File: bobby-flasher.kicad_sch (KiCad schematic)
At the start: 31 parts, among them J1 Conn_01x03, J2 Conn_01x06, J3 Flash, Q1 SS8050_C2150, Q2 SS8050_C2150, U1 CH343G, U2 AMS1117-3.3

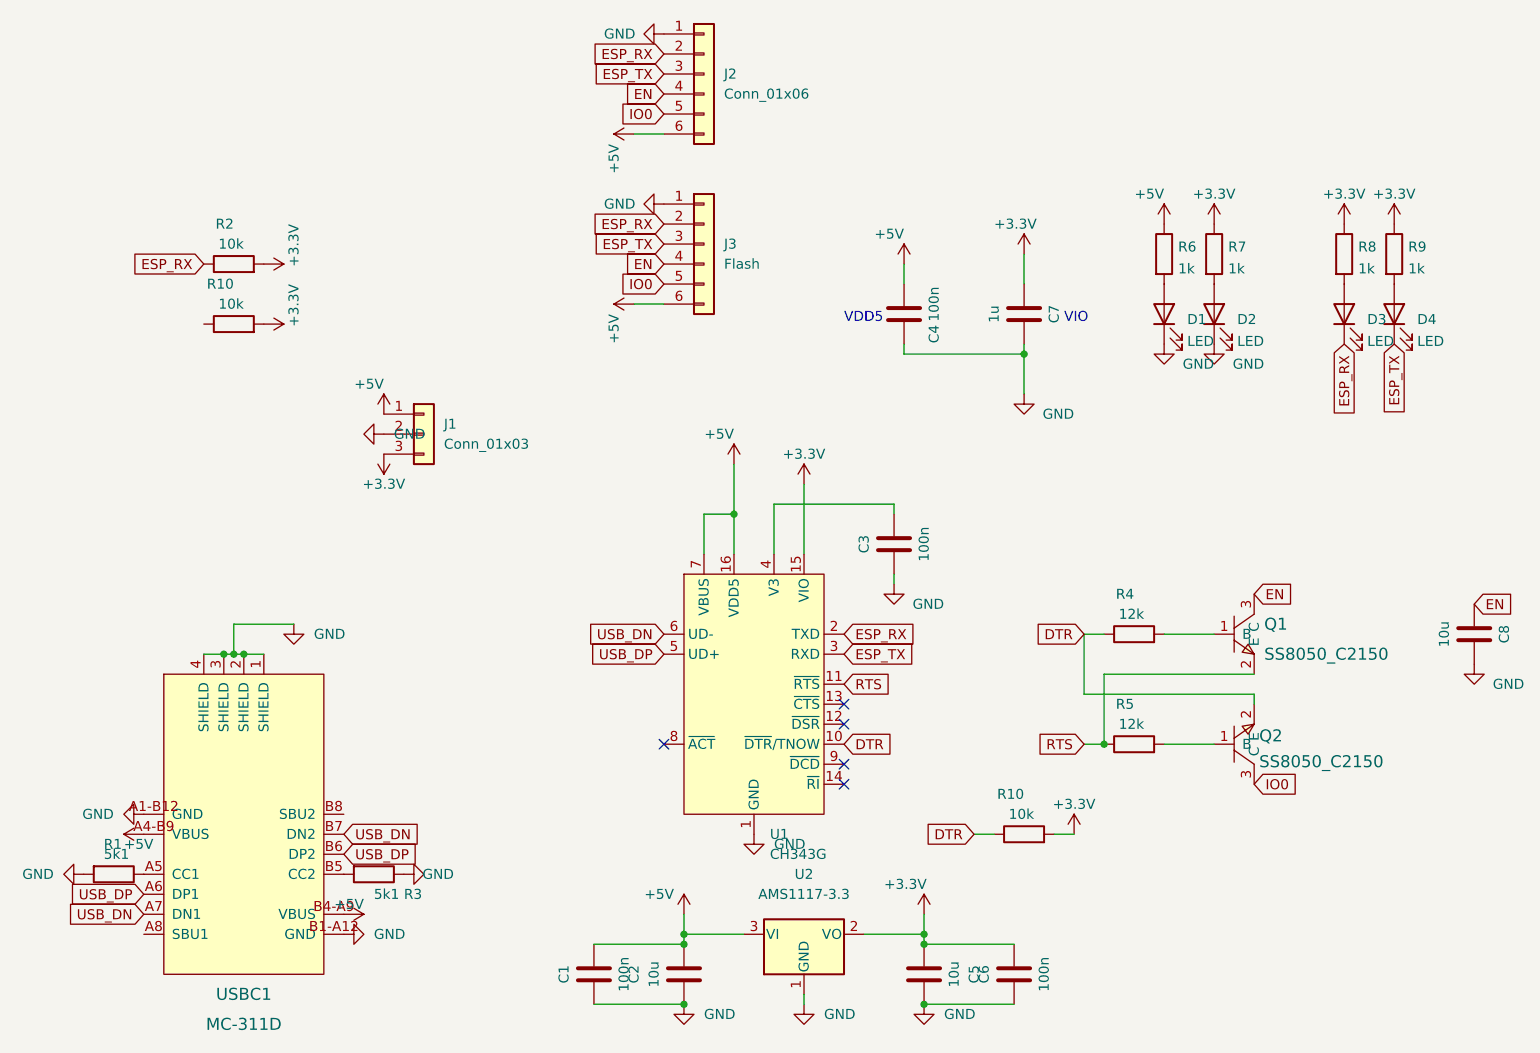
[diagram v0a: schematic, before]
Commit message: Ordered at JLCPCB; remove unconnected resistor from schematic; mark NPTH holes of USB-C as NPTH; fix connection of transistor in PCB file; replace unavailable LEDs with alternatives
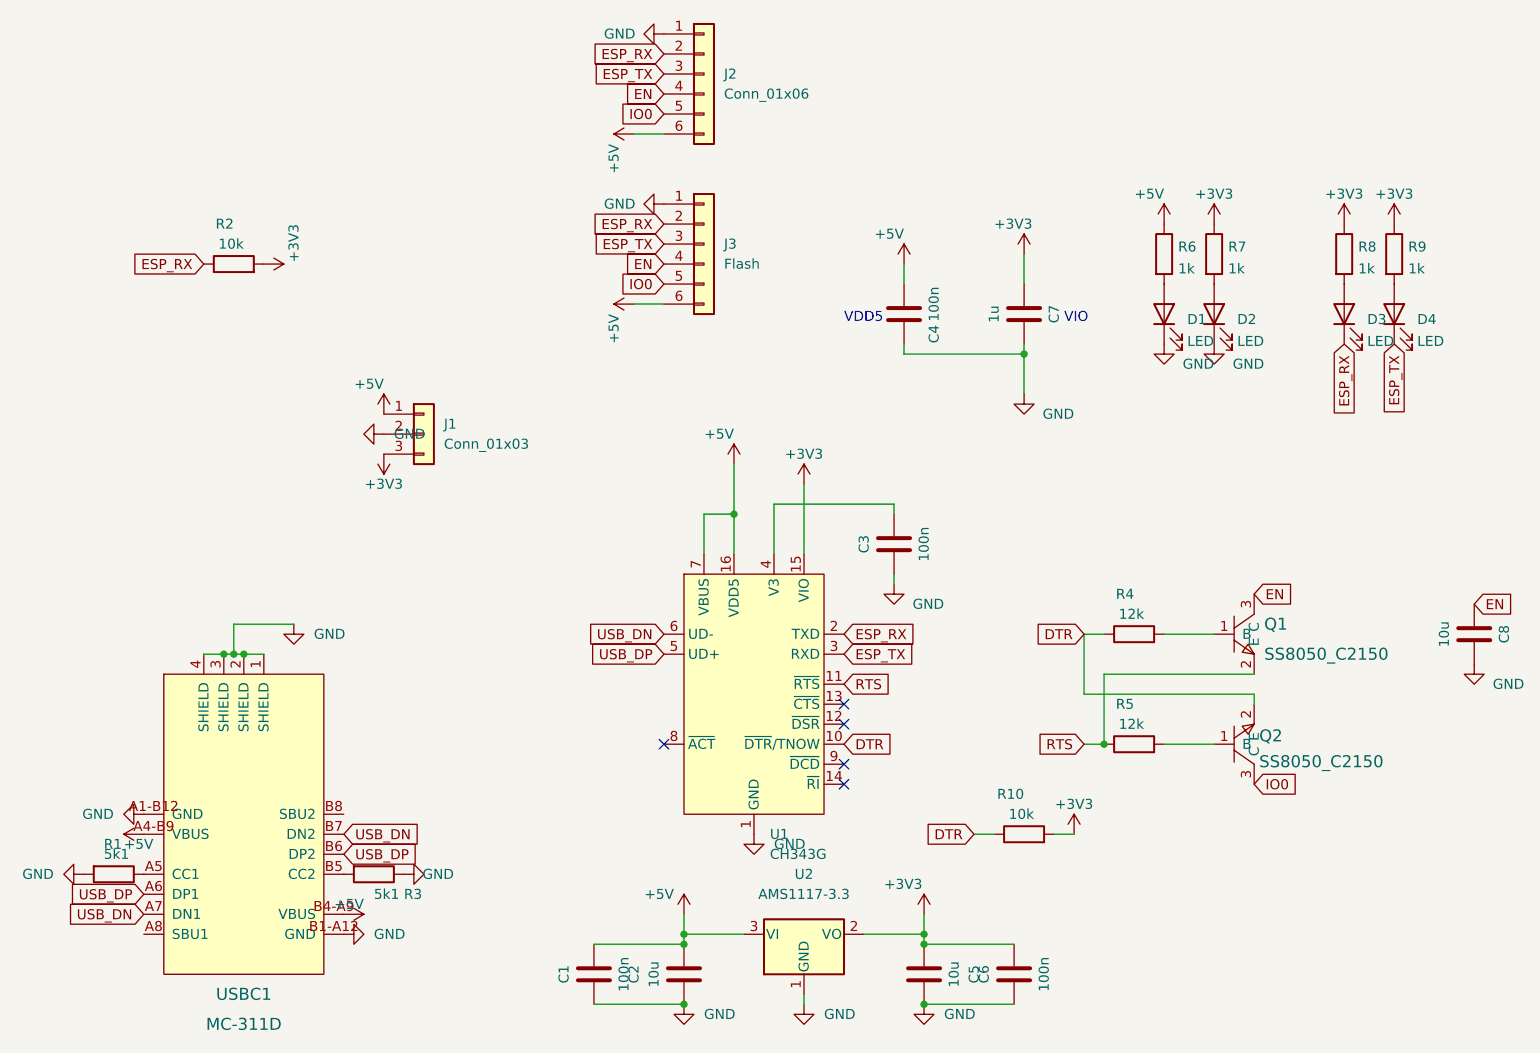
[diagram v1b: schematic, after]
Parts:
- removed R10: 10k, Resistor_SMD:R_0402_1005Metric, symbol Device:R
- D2: LCSC C72043 -> C965807
- D4: LCSC C72041 -> C965807
